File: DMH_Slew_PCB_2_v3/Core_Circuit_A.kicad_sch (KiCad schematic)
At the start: 60 parts, among them J1 TS_Jack_6.35mm_Sw, J11 Conn_02x03_Top_Bottom, J12 Conn_02x06_Top_Bottom, J13 Conn_02x03_Top_Bottom, J14 Conn_02x03_Top_Bottom, J15 Conn_02x06_Top_Bottom, J16 Conn_02x03_Top_Bottom, J17 Conn_01x08, J18 Conn_01x08, J19 Conn_01x08, J2 TS_Jack_6.35mm_Sw, J20 Conn_01x08, J3 TS_Jack_6.35mm_Sw, Q1 BC548, Q2 BC548, Q3 BC558, Q4 BC558, SW1 SW_DPDT_3way, SW2 SW_DPDT, SW3 SPDT_OnOffOn, U1 TL074, U2 TL074

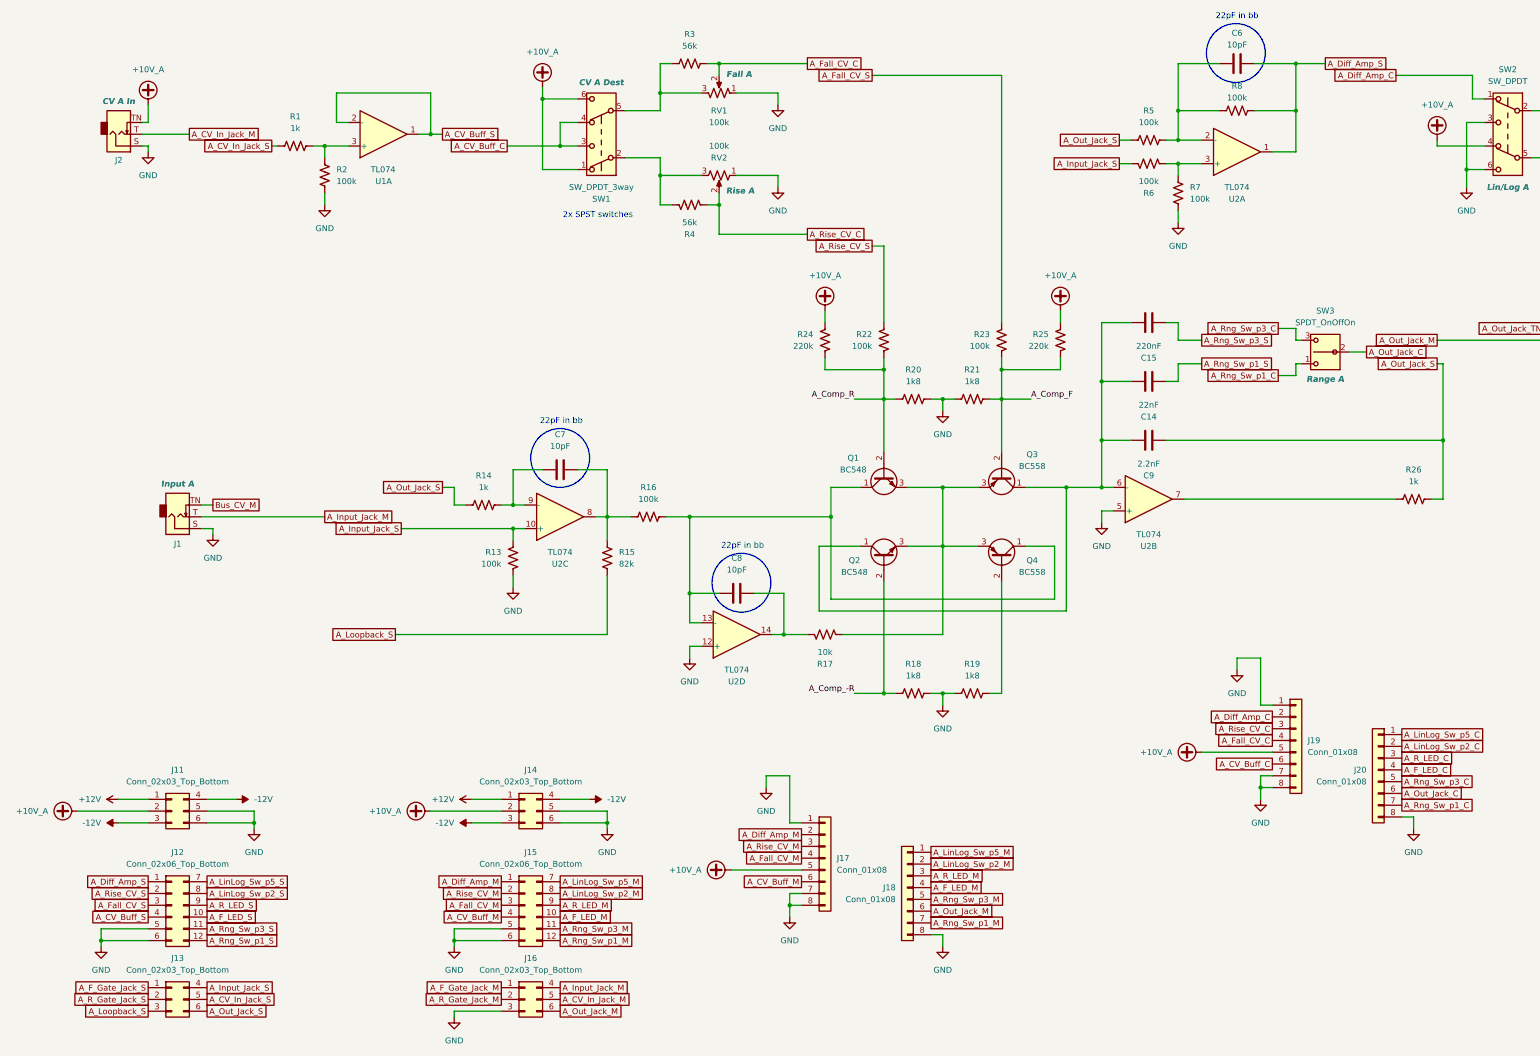
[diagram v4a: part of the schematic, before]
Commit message: Redesigned Main PCB
and regenerated Gerbers
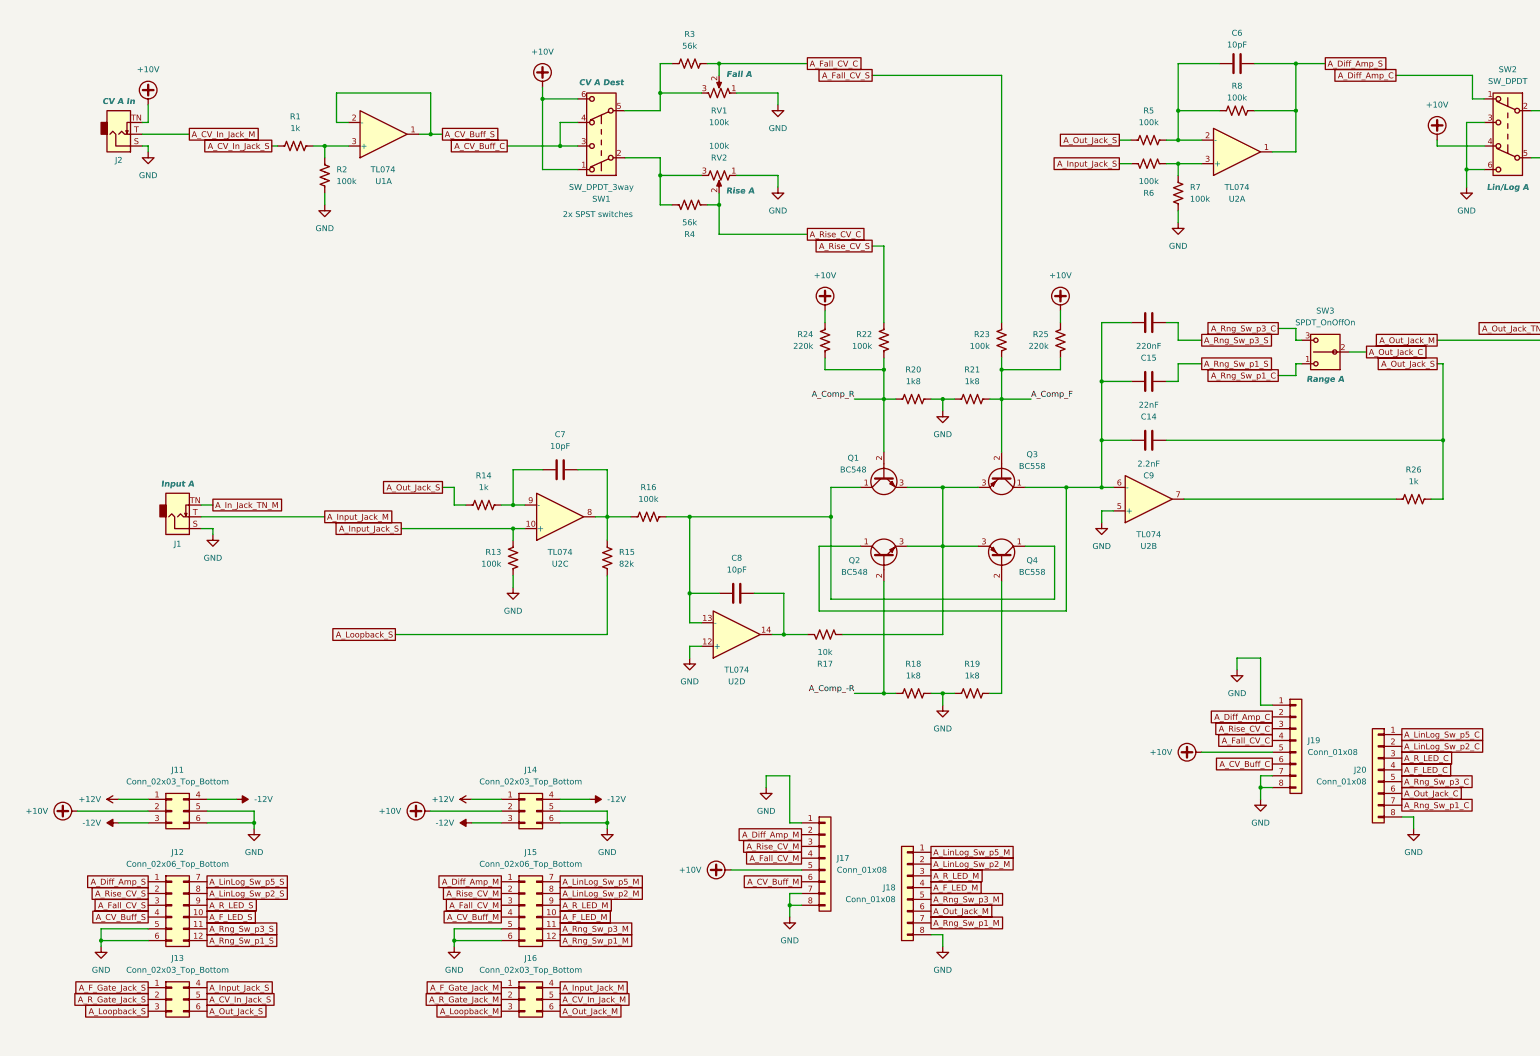
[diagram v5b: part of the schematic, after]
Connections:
- net GND: no longer J16.3 (Pin_3)
- net +10V_A renamed +10V
- net Bus_CV_M renamed A_In_Jack_TN_M
- new net A_Loopback_M: J16.3 (Pin_3)
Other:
- note removed: "22pF in bb"
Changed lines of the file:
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@@
 		(comment 1 "PCB for 5 cm Kosmo format synthesizer module")
 	)
-	(circle
-		(center 172.466 179.324)
-		(radius 6.35)
-		(stroke
-			(width 0)
-			(type default)
-		)
-		(fill
-			(type none)
-		)
-	)
-	(circle
-		(center 133.35 152.4)
-		(radius 6.35)
-		(stroke
-			(width 0)
-			(type default)
-		)
-		(fill
-			(type none)
-		)
-	)
-	(circle
-		(center 279.146 65.024)
-		(radius 6.35)
-		(stroke
-			(width 0)
-			(type default)
-		)
-		(fill
-			(type none)
-		)
-	)
-	(text "22pF in bb"
-		(exclude_from_sim no)
-		(at 279.4 57.15 0)
-		(effects
-			(font
-				(size 1.27 1.27)
-			)
-		)
-	)
 	(text "2x SPST switches"
 		(exclude_from_sim no)
@@
 		)
 	)
-	(text "22pF in bb"
-		(exclude_from_sim no)
-		(at 133.604 144.526 0)
-		(effects
-			(font
-				(size 1.27 1.27)
-			)
-		)
-	)
-	(text "22pF in bb"
-		(exclude_from_sim no)
-		(at 172.72 171.45 0)
-		(effects
-			(font
-				(size 1.27 1.27)
-			)
-		)
-	)
 	(junction
 		(at 154.94 91.44)
@@
 	(wire
 		(pts
-			(xy 110.49 271.78) (xy 110.49 273.05)
-		)
-		(stroke
-			(width 0)
-			(type default)
-		)
-	)
-	(wire
-		(pts
 			(xy 87.63 80.01) (xy 85.09 80.01)
 		)
@@
 	(wire
 		(pts
-			(xy 120.65 271.78) (xy 110.49 271.78)
-		)
-		(stroke
-			(width 0)
-			(type default)
-		)
-	)
-	(wire
-		(pts
 			(xy 133.35 85.09) (xy 137.16 85.09)
 		)
@@
 		)
 	)
+	(global_label "A_In_Jack_TN_M"
+		(shape passive)
+		(at 58.42 162.56 0)
+		(fields_autoplaced yes)
+		(effects
+			(font
+				(size 1.27 1.27)
+			)
+			(justify left)
+		)
+		(property "Intersheetrefs" "${INTERSHEET_REFS}"
+			(at 74.9895 162.56 0)
+			(effects
+				(font
+					(size 1.27 1.27)
+				)
+				(justify left)
+				(hide yes)
+			)
+		)
+	)
 	(global_label "A_Fall_CV_M"
 		(shape passive)
@@
 		)
 	)
-	(global_label "Bus_CV_M"
-		(shape passive)
-		(at 58.42 162.56 0)
-		(fields_autoplaced yes)
-		(effects
-			(font
-				(size 1.27 1.27)
-			)
-			(justify left)
-		)
-		(property "Intersheetrefs" "${INTERSHEET_REFS}"
-			(at 70.5975 162.56 0)
-			(effects
-				(font
-					(size 1.27 1.27)
-				)
-				(justify left)
-				(hide yes)
-			)
-		)
-	)
 	(global_label "A_Fall_CV_S"
 		(shape passive)
@@
 		)
 	)
+	(global_label "A_Loopback_M"
+		(shape passive)
+		(at 120.65 271.78 180)
+		(fields_autoplaced yes)
+		(effects
+			(font
+				(size 1.27 1.27)
+			)
+			(justify right)
+		)
+		(property "Intersheetrefs" "${INTERSHEET_REFS}"
+			(at 105.4111 271.78 0)
+			(effects
+				(font
+					(size 1.27 1.27)
+				)
+				(justify right)
+				(hide yes)
+			)
+		)
+	)
 	(global_label "A_CV_In_Jack_S"
 		(shape passive)
@@
 		(length 2.54)
 		(shape round)
+		(at 129.54 90.17 180)
+		(fields_autoplaced yes)
+		(effects
+			(font
+				(size 1.27 1.27)
+			)
+			(justify right bottom)
+		)
+		(property "Netclass" "Power"
+			(at 130.2385 92.71 0)
+			(effects
+				(font
+					(size 1.27 1.27)
+				)
+				(justify left)
+				(hide yes)
+			)
+		)
+		(property "Component Class" ""
+			(at 22.86 -87.63 0)
+			(effects
+				(font
+					(size 1.27 1.27)
+					(italic yes)
+				)
+			)
+		)
+	)
+	(netclass_flag ""
+		(length 2.54)
+		(shape round)
 		(at 30.48 64.77 0)
 		(fields_autoplaced yes)
@@
 			)
 		)
-		(property "Value" "+10V_A"
+		(property "Value" "+10V"
 			(at 322.58 76.2 0)
 			(effects
@@
 			)
 		)
-		(property "Value" "+10V_A"
+		(property "Value" "+10V"
 			(at 241.3 113.03 0)
 			(effects
@@
 			)
 		)
-		(property "Value" "+10V_A"
+		(property "Value" "+10V"
 			(at 265.43 215.8999 90)
 			(effects
@@
 			)
 		)
-		(property "Value" "+10V_A"
+		(property "Value" "+10V"
 			(at 129.54 64.77 0)
 			(effects
@@
 			)
 		)
-		(property "Value" "+10V_A"
+		(property "Value" "+10V"
 			(at 22.86 228.5999 90)
 			(effects
@@
 			)
 		)
-		(property "Value" "+10V_A"
+		(property "Value" "+10V"
 			(at 190.5 113.03 0)
 			(effects
@@
 			)
 		)
-		(property "Value" "+10V_A"
+		(property "Value" "+10V"
 			(at 163.83 241.2999 90)
 			(effects
@@
 			)
 		)
-		(property "Value" "+10V_A"
+		(property "Value" "+10V"
 			(at 44.45 68.58 0)
 			(effects
@@
 	)
 	(symbol
-		(lib_id "power:GND")
-		(at 110.49 273.05 0)
-		(mirror y)
-		(unit 1)
-		(exclude_from_sim no)
-		(in_bom yes)
-		(on_board no)
-		(dnp no)
-		(fields_autoplaced yes)
-		(property "Reference" "#PWR0102"
-			(at 110.49 279.4 0)
-			(effects
-				(font
-					(size 1.27 1.27)
-				)
-				(hide yes)
-			)
-		)
-		(property "Value" "GND"
-			(at 110.49 278.13 0)
-			(effects
-				(font
-					(size 1.27 1.27)
-				)
-			)
-		)
-		(property "Footprint" ""
-			(at 110.49 273.05 0)
-			(effects
-				(font
-					(size 1.27 1.27)
-				)
-				(hide yes)
-			)
-		)
-		(property "Datasheet" ""
-			(at 110.49 273.05 0)
-			(effects
-				(font
-					(size 1.27 1.27)
-				)
-				(hide yes)
-			)
-		)
-		(property "Description" "Power symbol creates a global label with name \"GND\" , ground"
-			(at 110.49 273.05 0)
-			(effects
-				(font
-					(size 1.27 1.27)
-				)
-				(hide yes)
-			)
-		)
-		(pin "1"
-		)
-		(instances
-			(project "DMH_Slew_PCB_2_v3"
-				(path "/58f4306d-5387-4983-bb08-41a2313fd315/7ad2d702-dfb7-4d49-a82d-34430dd5948f"
-					(reference "#PWR0102")
-					(unit 1)
-				)
-			)
-		)
-	)
-	(symbol
 		(lib_id "SynthStuff:SW_SPDT_OnOffOn")
 		(at 298.45 129.54 180)
@@
 			)
 		)
-		(property "Value" "+10V_A"
+		(property "Value" "+10V"
 			(at 99.06 228.5999 90)
 			(effects

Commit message: Cleaned up old breadboarding notes
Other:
- note removed: "2x SPST switches"
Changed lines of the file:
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@@
 		(comment 1 "PCB for 5 cm Kosmo format synthesizer module")
-	)
-	(text "2x SPST switches"
-		(exclude_from_sim no)
-		(at 141.478 100.076 0)
-		(effects
-			(font
-				(size 1.27 1.27)
-			)
-		)
 	)
 	(junction
